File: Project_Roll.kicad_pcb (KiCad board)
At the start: 4 copper layers, 98.2 x 120.8 mm, 70 parts, among them J1 TB002-500-02BE, J10 Conn_01x04, J11 Conn_01x04, J12 Conn_01x02, J13 TB002-500-02BE, J14 TB002-500-02BE, J15 TB002-500-02BE, J16 TB002-500-02BE, J2 TB002-500-02BE, J3 TB002-500-02BE, J4 TB002-500-02BE, J5 TB002-500-02BE, J6 Conn_01x05, J7 Conn_01x05, J8 Conn_01x04, J9 Conn_01x04, Q1 IRFS7430TRLPBF, U1 AP62300TWU, U2 GY-521, U3 ESP32-DEVKIT-V1

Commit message: TVS Diode fix and layout changes
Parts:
- moved D2 35.0 mm to (148.8, 153.2), turned to 180 degrees
- moved C2 18.0 mm to (138.0, 121.5), turned to 90 degrees
- moved D3 3.31 mm to (151.2, 125.2)
- moved R1 3.25 mm to (145.0, 126.0)
- moved Q1 3.10 mm to (148.5, 136.4)
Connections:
- D2 pad 2: GND -> GND_BAT
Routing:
- net +12V: track 15.8 -> 16.1 mm, vias 0 -> 15

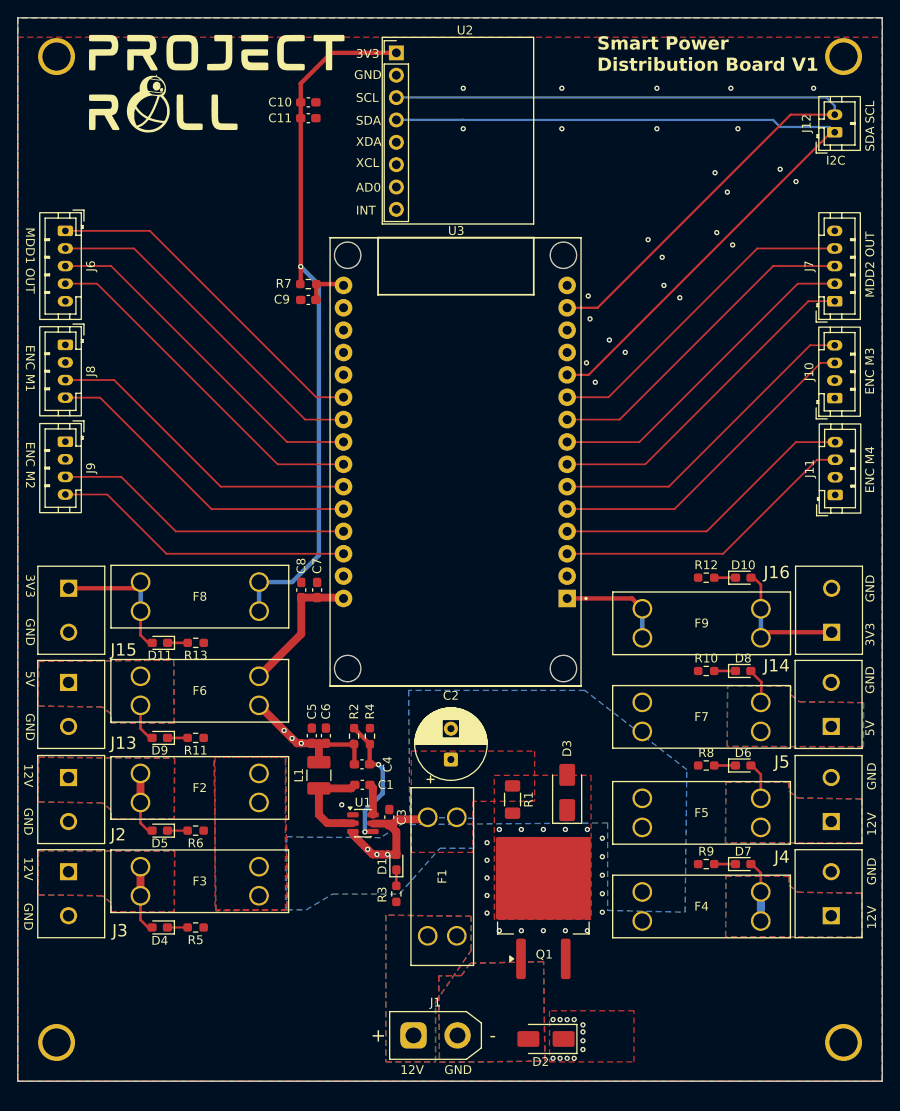
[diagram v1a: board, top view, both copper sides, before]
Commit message: Vias for power connections
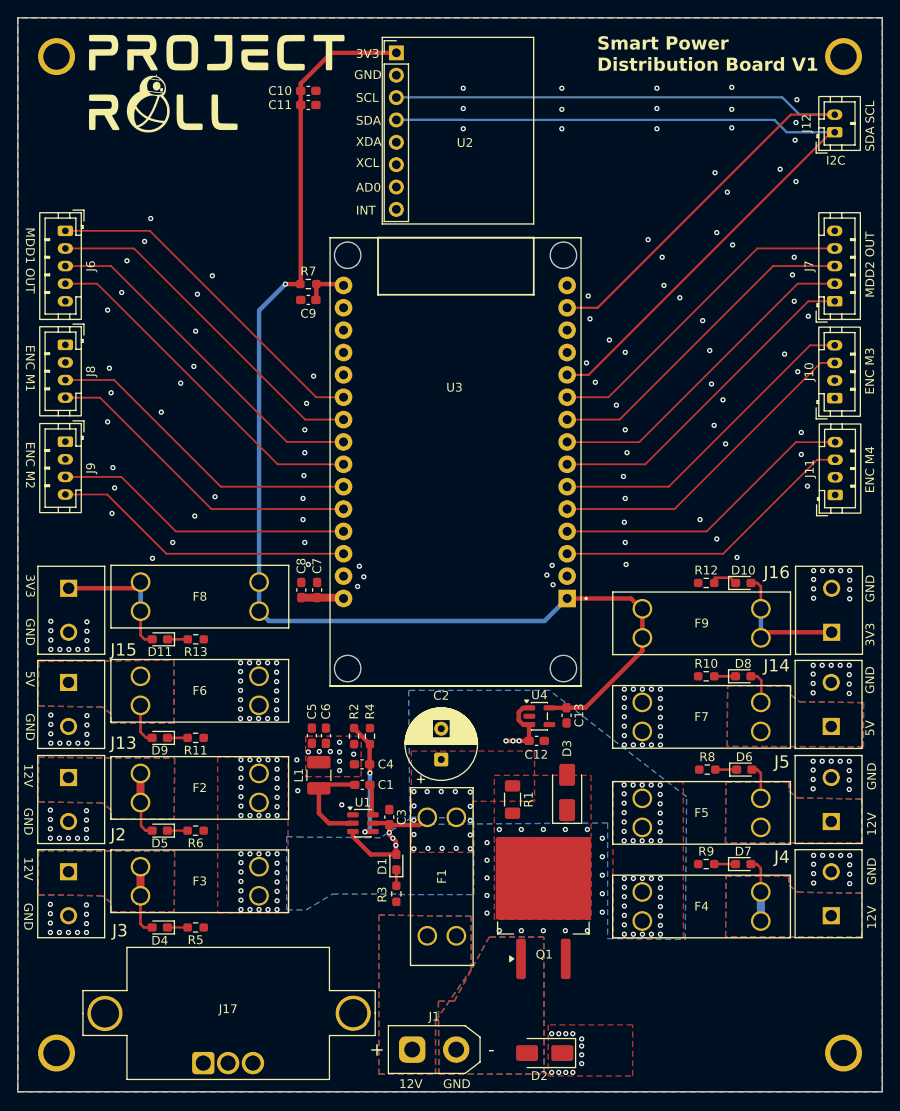
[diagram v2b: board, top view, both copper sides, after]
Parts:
- added C12: 1uF, Capacitor_SMD:C_0603_1608Metric_Pad1.08x0.95mm_HandSolder, F.Cu at (147.7, 119.3)
- added C13: 1uF, Capacitor_SMD:C_0603_1608Metric_Pad1.08x0.95mm_HandSolder, F.Cu at (151.1, 116.4)
- added G***: LOGO, BB8 Footprints:asher, B.Cu at (110.5, 51.0)
- added J17: Conn_01x03, BB8 Footprints:Voltage Meter, F.Cu at (112.7, 150.3)
- added U4: MIC5504-3.3YM5, Package_TO_SOT_SMD:SOT-23-5, F.Cu at (148.1, 116.5)
- moved D2 1.61 mm to (148.7, 154.8)
- moved J1 1.61 mm to (138.6, 154.4)
- moved C11 1.50 mm to (121.8, 47.1)
- moved C10 1.30 mm to (121.8, 45.5)
- moved H3 1.20 mm to (93.2, 154.8)
- moved H4 1.20 mm to (182.6, 154.8)
- moved C2 1.10 mm to (136.9, 121.5)
- moved D8 0.60 mm to (171.2, 112.0)
- moved R10 0.60 mm to (167.0, 112.0)
- moved D10 0.60 mm to (171.2, 101.4)
- moved R12 0.60 mm to (167.0, 101.4)
- moved D6 0.48 mm to (171.3, 122.6)
- moved R8 0.48 mm to (167.1, 122.6)
- moved D11 0.40 mm to (104.9, 107.8)
- moved R13 0.40 mm to (109.0, 107.8)
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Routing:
- net +5V: track 33.6 -> 13.8 mm, vias 3 -> 51
- net Net-(U1-FB): track 15.6 -> 14.0 mm
- net +3V3: track 137.9 -> 139.2 mm
- net +12V: track 16.1 -> 17.0 mm, vias 15 -> 111
- net I2C_SCL: track 90.7 -> 90.1 mm
- net GND: vias 41 -> 199
- added copper zone on F.Cu, net +5V
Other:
- board size 98.2 x 120.8 mm -> 98.2 x 122 mm

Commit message: fixed 5v fill
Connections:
- U3 pad 1: +3V3 -> unconnected-(U3-3V3-Pad1)
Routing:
- net +3V3: track 139.2 -> 138.0 mm
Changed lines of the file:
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@@
 		)
 		(embedded_fonts no)
+		(model "${KICAD10_3DMODEL_DIR}/Sensor_Voltage.3dshapes/LEM_LV25-P.step"
+			(offset
+				(xyz -9 4.5 0)
+			)
+			(scale
+				(xyz 0.8 0.58 0.4)
+			)
+			(rotate
+				(xyz -0 -0 -0)
+			)
+		)
 	)
 	(footprint "Capacitor_SMD:C_0603_1608Metric_Pad1.08x0.95mm_HandSolder"
@@
 			(layers "*.Cu" "*.Mask")
 			(remove_unused_layers no)
-			(net "+3V3")
+			(net "unconnected-(U3-3V3-Pad1)")
 			(pinfunction "3V3_1")
-			(pintype "output")
+			(pintype "output+no_connect")
 			(solder_mask_margin 0.102)
 		)
@@
 	)
 	(segment
-		(start 131.8 132.2375)
-		(end 128.8875 132.2375)
-		(width 0.5)
-		(layer "F.Cu")
-		(net "+12V")
-	)
-	(segment
 		(start 131 128.8625)
 		(end 131.0375 128.9)
@@
 	)
 	(segment
-		(start 126.86297 130.21297)
-		(end 126.86297 129.636051)
+		(start 131.8 132.2375)
+		(end 128.5375 132.2375)
 		(width 0.5)
 		(layer "F.Cu")
@@
 	)
 	(segment
+		(start 128.5375 132.2375)
+		(end 126.86297 130.56297)
+		(width 0.5)
+		(layer "F.Cu")
+		(net "+12V")
+	)
+	(segment
 		(start 131 129.75)
 		(end 131 130)
@@
 	)
 	(segment
-		(start 131.75 131.2)
-		(end 131.75 132.1875)
+		(start 126.86297 130.56297)
+		(end 126.86297 129.636051)
 		(width 0.5)
 		(layer "F.Cu")
@@
 	)
 	(segment
-		(start 128.8875 132.2375)
-		(end 126.86297 130.21297)
+		(start 131.75 131.2)
+		(end 131.75 132.1875)
 		(width 0.5)
 		(layer "F.Cu")
@@
 	)
 	(via
+		(at 112.6 89.1)
+		(size 0.6)
+		(drill 0.3)
+		(layers "F.Cu" "B.Cu")
+		(free yes)
+		(net "GND")
+	)
+	(via
 		(at 93.525 141.1)
 		(size 0.6)
@@
 	)
 	(via
-		(at 105.1 82)
-		(size 0.6)
-		(drill 0.3)
-		(layers "F.Cu" "B.Cu")
-		(free yes)
-		(net "GND")
-	)
-	(via
 		(at 92.5 141.1)
 		(size 0.6)
@@
 	)
 	(segment
-		(start 158.46 103.16)
-		(end 151.20047 103.16)
+		(start 120.9375 45.5)
+		(end 120.9375 44.6625)
 		(width 0.5)
 		(layer "F.Cu")
@@
 	)
 	(segment
-		(start 120.9375 45.5)
-		(end 120.9375 44.6625)
+		(start 120.9375 67.39547)
+		(end 120.9375 47.1)
 		(width 0.5)
 		(layer "F.Cu")
@@
 	)
 	(segment
-		(start 159.7505 104.3318)
-		(end 159.6318 104.3318)
+		(start 158.6823 105.4)
+		(end 117.0081 105.4)
 		(width 0.5)
 		(layer "F.Cu")
@@
 	)
 	(segment
-		(start 120.9375 67.39547)
-		(end 120.9375 47.1)
+		(start 119.2 67.45)
+		(end 120.88297 67.45)
 		(width 0.5)
 		(layer "F.Cu")
@@
 	)
 	(segment
-		(start 119.2 67.45)
-		(end 120.88297 67.45)
+		(start 117.0081 105.4)
+		(end 116.2101 104.602)
 		(width 0.5)
 		(layer "F.Cu")
@@
 	)
 	(segment
-		(start 120.9375 44.6625)
-		(end 124.42 41.18)
+		(start 159.7505 104.3318)
+		(end 158.6823 105.4)
 		(width 0.5)
 		(layer "F.Cu")
@@
 	)
 	(segment
-		(start 120.9375 47.1)
-		(end 120.9375 45.5)
+		(start 120.9375 44.6625)
+		(end 124.42 41.18)
 		(width 0.5)
 		(layer "F.Cu")
@@
 	)
 	(segment
-		(start 159.6318 104.3318)
-		(end 158.46 103.16)
+		(start 120.9375 47.1)
+		(end 120.9375 45.5)
 		(width 0.5)
 		(layer "F.Cu")
@@
 	)
 	(segment
-		(start 148.64087 105.7196)
-		(end 117.3277 105.7196)
-		(width 0.5)
-		(layer "B.Cu")
-		(net "+3V3")
-	)
-	(segment
 		(start 116.2101 70.4399)
 		(end 119.2 67.45)
@@
 	)
 	(segment
-		(start 117.3277 105.7196)
-		(end 116.2101 104.602)
-		(width 0.5)
-		(layer "B.Cu")
-		(net "+3V3")
-	)
-	(segment
-		(start 151.20047 103.16)
-		(end 148.64087 105.7196)
-		(width 0.5)
-		(layer "B.Cu")
-		(net "+3V3")
-	)
-	(segment
 		(start 102.8 129)
 		(end 102.8 126.39733)
@@
 		(layer "F.Cu")
 		(hatch edge 0.5)
+		(priority 4)
+		(connect_pads yes
+			(clearance 0.5)
+		)
+		(min_thickness 0.25)
+		(fill yes
+			(thermal_gap 0.5)
+			(thermal_bridge_width 0.5)
+			(island_removal_mode 0)
+		)
+		(polygon
+			(pts
+				(xy 161.2 113.1) (xy 156.4 113.1) (xy 156.4 120.074791) (xy 164.397304 120.074791) (xy 164.3955 113.099174)
+			)
+		)
+	)
+	(zone
+		(net "+5V")
+		(layer "F.Cu")
+		(hatch edge 0.5)
 		(priority 9)
 		(connect_pads yes
@@
 			)
 		)
+	)
+	(zone
+		(net "+5V")
+		(layer "F.Cu")
+		(hatch edge 0.5)
+		(priority 4)
+		(connect_pads yes
+			(clearance 0.5)
+		)
+		(min_thickness 0.25)
+		(fill yes
+			(thermal_gap 0.5)
+			(thermal_bridge_width 0.5)
+			(island_removal_mode 0)
+		)
+		(polygon
+			(pts
+				(xy 114.6 117.074791) (xy 119.4 117.074791) (xy 119.4 110.1) (xy 111.402696 110.1) (xy 111.4045 117.075617)
+			)
+		)

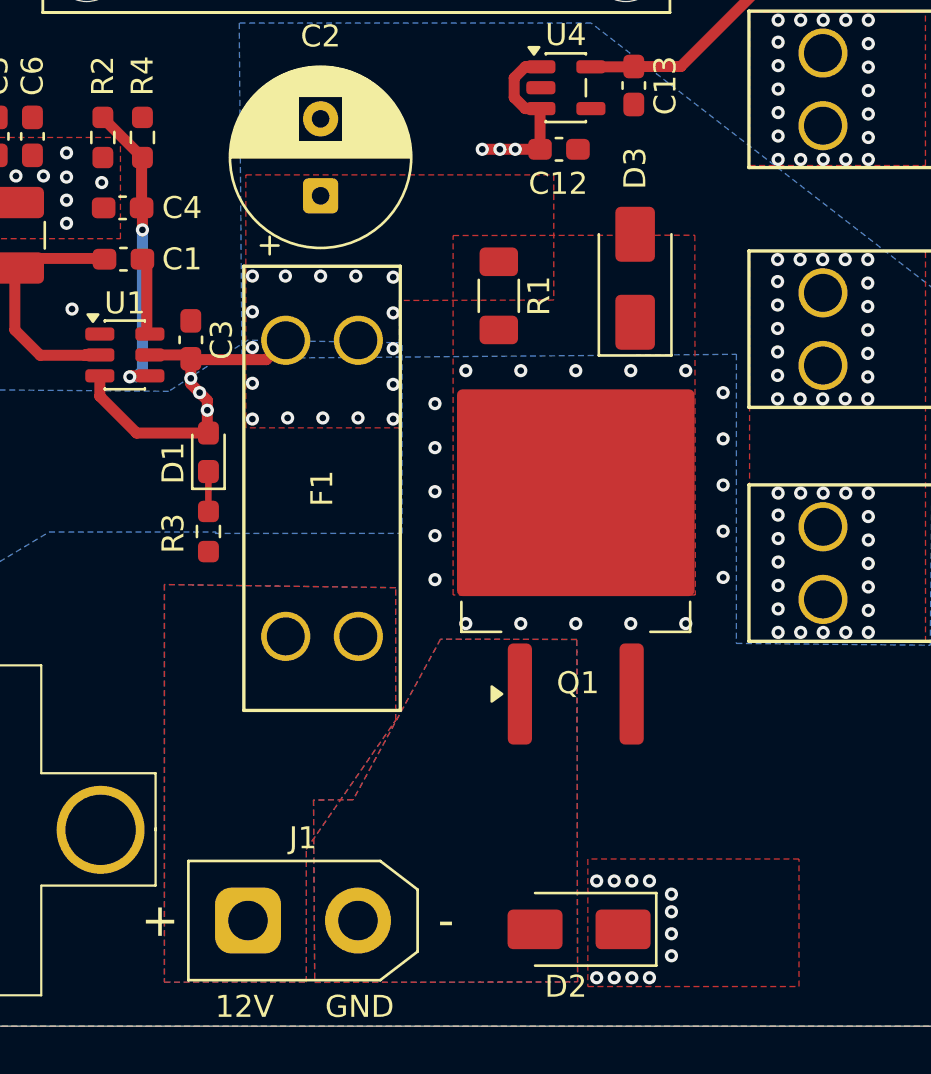
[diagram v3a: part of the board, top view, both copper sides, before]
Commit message: cleaned up fills
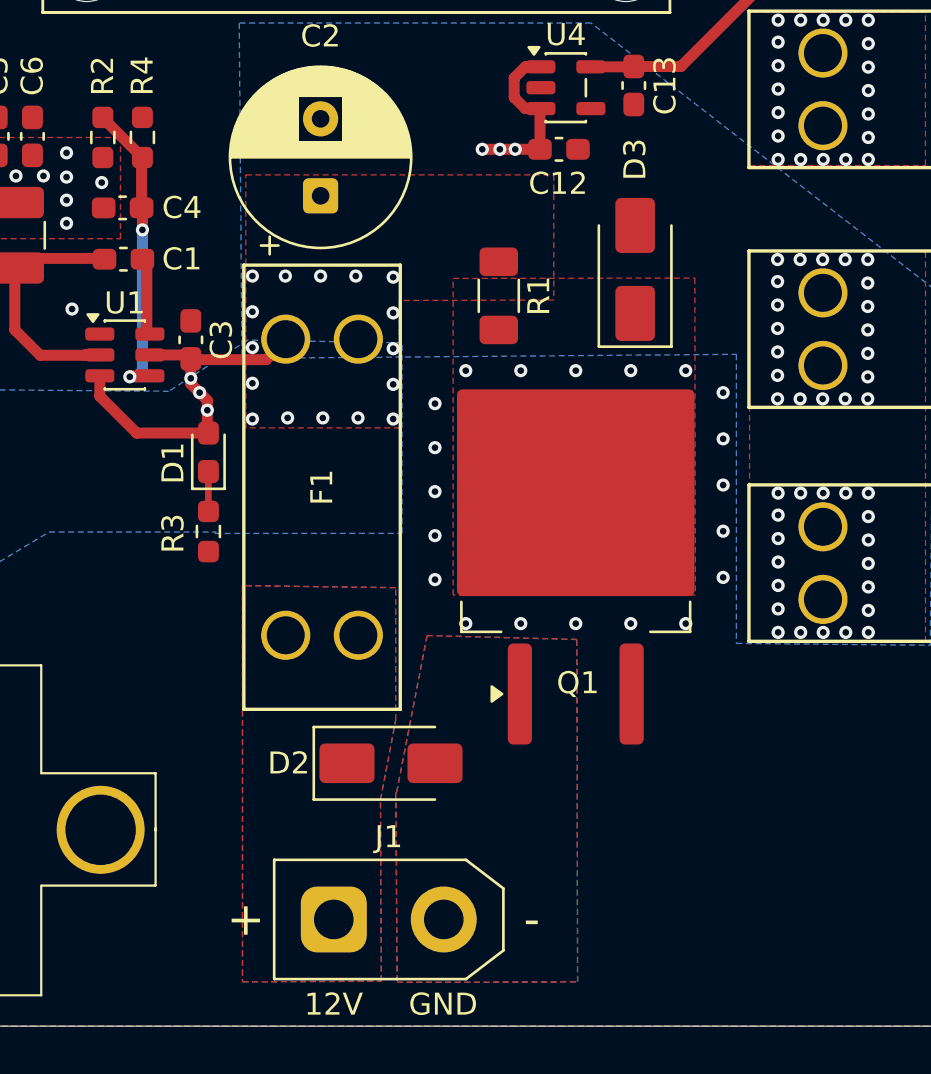
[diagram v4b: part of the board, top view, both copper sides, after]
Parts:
- moved D2 11.4 mm to (140.1, 147.2), turned to 0 degrees
- moved J1 3.90 mm to (142.5, 154.3)
- moved D3 0.40 mm to (151.2, 124.8)
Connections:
- D2 pad 1: +12V -> V_BATT
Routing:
- net +12V: vias 111 -> 99
